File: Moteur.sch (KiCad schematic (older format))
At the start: 56 parts, among them IC1 TPS71501, IC2 TLV710, IC3 MAX3051, IC4 LM5106, IC5 LM5106, IC6 INA282, P1 Bus2, P2 MotorEnc, P3 Bus1, P4 Motor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

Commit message: final schematic review, component placement
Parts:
- removed D2: DEL_RGB, ~, symbol DEL_RGB
- removed JP1: JUMPER, ~, symbol JUMPER
- removed P2: MotorEnc, symbol CONN_5
- removed P3: Bus1, symbol CONN_4
- removed P4: Motor, symbol CONN_2
- removed P6: PWR, symbol CONN_2
- removed P7: GPIO, ~, symbol CONN_5
- removed R7: 120, ~, symbol R
- added D2: LED, ~, symbol LED
- added P2: CONN_6, ~, symbol CONN_6
- added P3: GPIO, ~, symbol CONN_6
- added P4, P6: CONN_1, ~, symbol CONN_1
- R3: value 0R -> 10k
- R5: value 47 -> 10k
- R6: value 39 -> 10k
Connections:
- net labels added: CAN_SPEED, LED
- net labels removed: ADC/I_BAT, LEDB, LEDG, LEDR
- wire segments 183 -> 178
- no-connect marks 14 -> 16
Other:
- moved on the sheet: C17, P1, R4

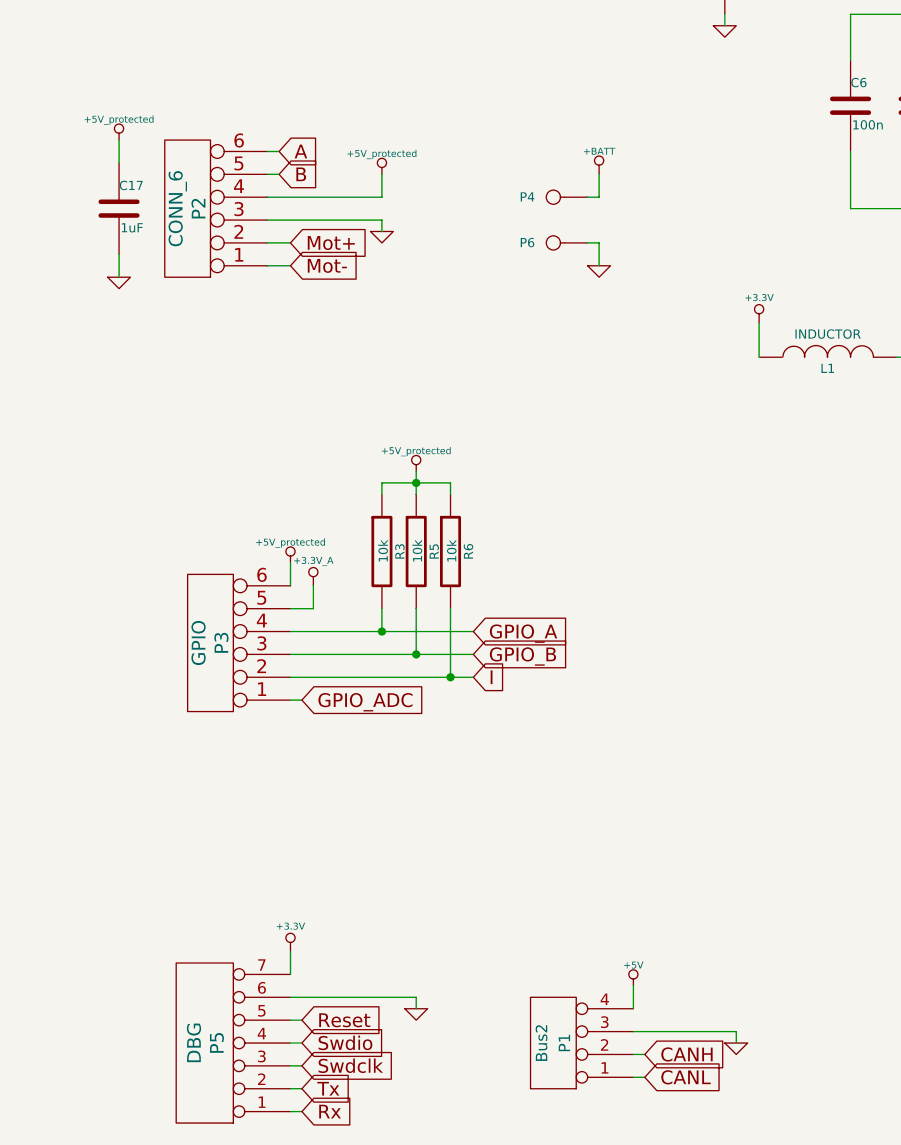
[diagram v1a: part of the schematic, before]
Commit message: add GND to GPIO connector, exchange CANL,CANH
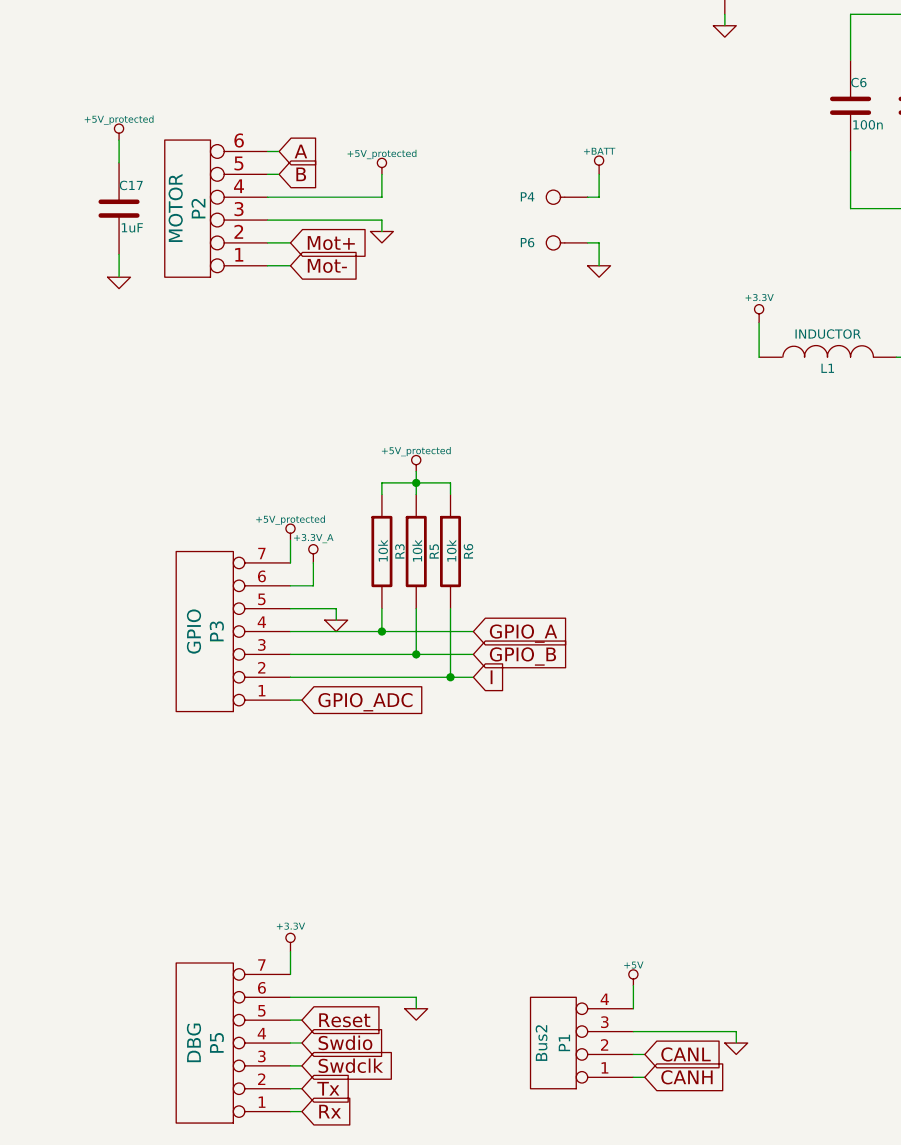
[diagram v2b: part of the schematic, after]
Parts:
- removed P3: GPIO, ~, symbol CONN_6
- added P3: GPIO, ~, symbol CONN_7
- P2: value CONN_6 -> MOTOR
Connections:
- wire segments 178 -> 180

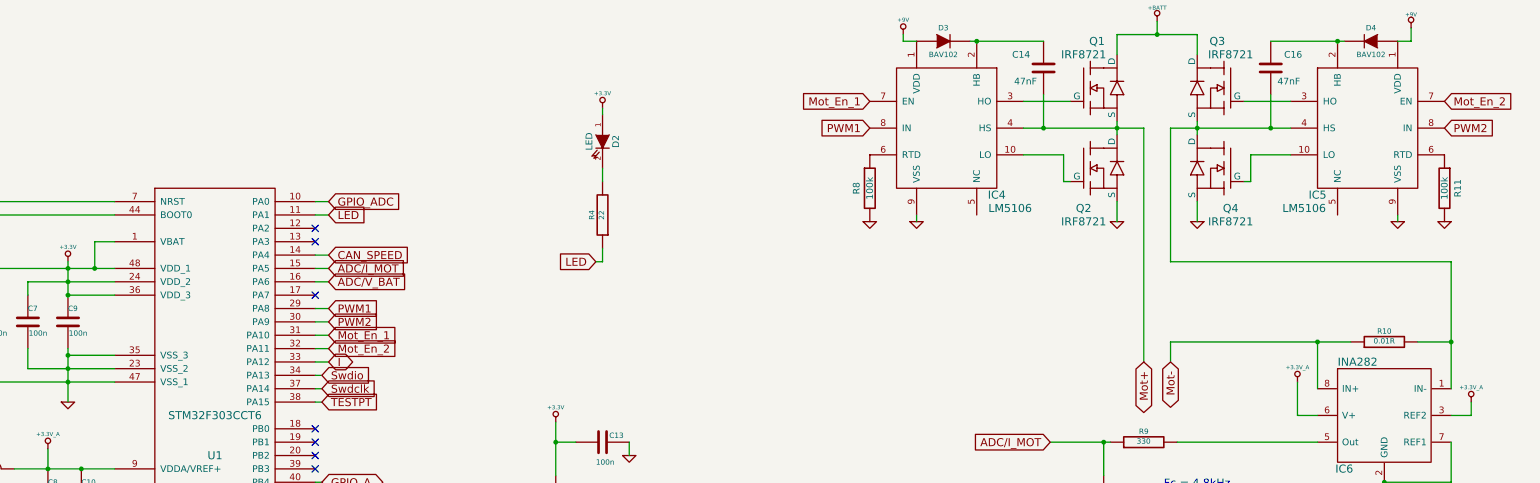
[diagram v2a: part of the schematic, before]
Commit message: exchange shunt resistance pins
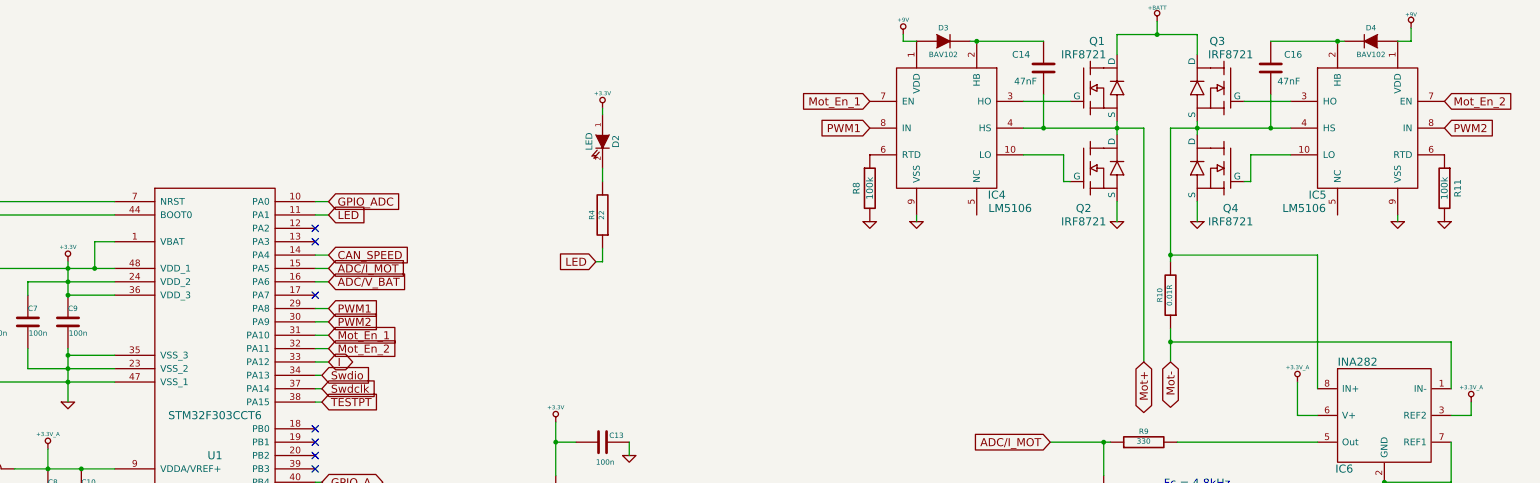
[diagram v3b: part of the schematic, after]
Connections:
- wire segments 180 -> 179
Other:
- moved on the sheet: R10
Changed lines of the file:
@@
 Sheet 1 1
 Title "Motor control board"
-Date "28 nov 2014"
+Date "3 dec 2014"
 Rev "V00"
 Comp "CVRA"
@@
 L R R10
 U 1 1 545545D1
-P 14350 5150
-F 0 "R10" V 14430 5150 40  0000 C CNN
-F 1 "0.01R" V 14357 5151 40  0000 C CNN
-F 2 "~" V 14280 5150 30  0000 C CNN
-F 3 "~" H 14350 5150 30  0000 C CNN
-	1    14350 5150
-	0    -1   -1   0
+P 12750 4800
+F 0 "R10" V 12830 4800 40  0000 C CNN
+F 1 "0.01R" V 12757 4801 40  0000 C CNN
+F 2 "~" V 12680 4800 30  0000 C CNN
+F 3 "~" H 12750 4800 30  0000 C CNN
+	1    12750 4800
+	-1   0    0    1
 $EndComp
 Text GLabel 10500 3350 0    60   Input ~ 0
@@
 Connection ~ 4700 4600
 Wire Wire Line
-	4700 4400 4700 4600
-Wire Wire Line
-	4850 4400 4700 4400
+	4700 4600 4700 4400
+Wire Wire Line
+	4700 4400 4850 4400
 Wire Wire Line
 	6400 6900 6350 6900
@@
 Wire Wire Line
 	10750 2900 10850 2900
-Connection ~ 14850 5150
-Wire Wire Line
-	12750 4550 14850 4550
-Connection ~ 13850 5150
-Wire Wire Line
-	12750 5150 12750 5300
-Wire Wire Line
-	14850 4550 14850 5500
-Wire Wire Line
-	14600 5150 14850 5150
-Wire Wire Line
-	13850 5150 13850 5500
-Wire Wire Line
-	12750 5150 14100 5150
+Wire Wire Line
+	12750 5050 12750 5300
 Wire Wire Line
 	950  2300 950  2500
@@
 Connection ~ 13500 3550
 Wire Wire Line
-	13500 3300 13500 3550
+	13500 3550 13500 3300
 Wire Wire Line
 	14550 2800 14550 2900
@@
 Wire Wire Line
 	1650 7200 1450 7200
+Connection ~ 12750 5150
+Wire Wire Line
+	14850 5500 14850 5150
+Wire Wire Line
+	14850 5150 12750 5150
+Wire Wire Line
+	13850 5500 13850 4500
+Wire Wire Line
+	13850 4500 12750 4500
+Connection ~ 12750 4500
 $EndSCHEMATC
